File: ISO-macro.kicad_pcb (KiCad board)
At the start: 2 copper layers, 105.9 x 38.1 mm, 20 parts, among them J1 USB_C_Receptacle_USB2.0, SW1 SW_SPST, SW2 SW_SPST, SW3 SW_SPST, SW4 SW_SPST, SW5 SW_SPST, SW6 SW_SPST, SW7 SW_SPST, SW8 Rotary_Encoder_Switch, SW9 SW_SPST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

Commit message: add backlights, connect things
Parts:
- added C2: 100n, Capacitor_SMD:C_0402_1005Metric, B.Cu at (129.0, 75.3)
- added C3: 100n, Capacitor_SMD:C_0402_1005Metric, B.Cu at (129.0, 79.4)
- added C4: 100nF, Capacitor_SMD:C_0402_1005Metric, B.Cu at (141.6, 77.0)
- added C5: 100nF, Capacitor_SMD:C_0402_1005Metric, B.Cu at (173.0, 77.2)
- added C6: 100nF, Capacitor_SMD:C_0402_1005Metric, B.Cu at (188.0, 77.6)
- added D1: WS2812B, LED_SMD:LED_WS2812B_PLCC4_5.0x5.0mm_P3.2mm, B.Cu at (136.3, 77.3)
- added D2: WS2812B, LED_SMD:LED_WS2812B_PLCC4_5.0x5.0mm_P3.2mm, B.Cu at (168.1, 77.3)
- added D3: WS2812B, LED_SMD:LED_WS2812B_PLCC4_5.0x5.0mm_P3.2mm, B.Cu at (192.4, 77.3)
- added R7: 10k, Resistor_SMD:R_0402_1005Metric, B.Cu at (117.5, 74.9)
- added R8: 10k, Resistor_SMD:R_0402_1005Metric, B.Cu at (117.5, 79.9)
- SW8: value Rotary_Encoder_Switch -> EC11
- moved SW9 3.78 mm to (186.5, 71.6)
- moved R4 0.67 mm to (120.3, 92.1)
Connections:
- SW8 pad A: Net-(SW8-PadA) -> /EncA
- SW8 pad B: Net-(SW8-PadB) -> /EncB
- SW8 pad C: Net-(SW8-PadC) -> GND
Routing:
- net VCC: track 83.9 -> 172.2 mm
- net GND: track 43.1 -> 87.2 mm
- net Net-(D1-Pad2): track 0.00 -> 28.3 mm
- net Net-(D2-Pad2): track 0.00 -> 20.7 mm
- net /EncB: track 0.00 -> 11.1 mm, vias 0 -> 1
- net /EncA: track 0.00 -> 11.1 mm, vias 0 -> 1
- net /Reset: track 70.9 -> 74.6 mm
- net Net-(R4-Pad2): track 1.57 -> 2.24 mm
- net Net-(SW2-Pad2): track 37.3 -> 37.9 mm
- net Net-(SW4-Pad2): track 54.0 -> 54.5 mm

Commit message: updated MCU, removed filter for rot enc
updated MCU, removed filter for rot enc
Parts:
- removed C2, C3: 100n, Capacitor_SMD:C_0402_1005Metric
- removed R7, R8: 10k, Resistor_SMD:R_0402_1005Metric
- U1: value ATmega16U4-MU -> ATmega16U2-MU; footprint Package_DFN_QFN:QFN-44-1EP_7x7mm_P0.5mm_EP5.2x5.2mm -> Package_DFN_QFN:QFN-32-1EP_5x5mm_P0.5mm_EP3.1x3.1mm
- moved U1 0.06 mm to (125.5, 88.6), turned to 0 degrees
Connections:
- R4 pad 1: GND -> /LED
- SW8 pad S2: Net-(SW8-PadS2) -> /encsw
- U1 pad 1: Net-(U1-Pad1) -> /Res1
- U1 pad 13: /Reset -> Net-(R4-Pad2)
- U1 pad 14: VCC -> Net-(SW7-Pad2)
- U1 pad 15: GND -> Net-(SW6-Pad2)
- U1 pad 16: /Res2 -> Net-(SW4-Pad2)
- U1 pad 17: /Res1 -> Net-(U1-Pad17)
- U1 pad 19: Net-(U1-Pad19) -> Net-(SW2-Pad2)
- U1 pad 2: VCC -> /Res2
- U1 pad 20: Net-(U1-Pad20) -> /encsw
- U1 pad 23: GND -> Net-(SW1-Pad2)
- U1 pad 24: VCC -> /Reset
- U1 pad 25: Net-(SW1-Pad2) -> Net-(U1-Pad25)
- U1 pad 26: Net-(SW3-Pad2) -> /EncB
- U1 pad 27: Net-(SW5-Pad2) -> Net-(C1-Pad1)
- U1 pad 28: Net-(SW7-Pad2) -> GND
- U1 pad 29: Net-(SW6-Pad2) -> Net-(R2-Pad1)
- U1 pad 3: Net-(R3-Pad1) -> GND
- U1 pad 30: Net-(SW4-Pad2) -> Net-(R3-Pad1)
- U1 pad 31: Net-(SW2-Pad2) -> VCC
- U1 pad 32: Net-(SW8-PadS2) -> VCC
- U1 pad 33: Net-(R4-Pad2) -> GND
- U1 pad 4: Net-(R2-Pad1) -> VCC
- U1 pad 5: GND -> /EncA
- U1 pad 6: Net-(C1-Pad1) -> Net-(SW3-Pad2)
- U1 pad 7: VCC -> Net-(SW5-Pad2)
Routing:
- net /LED: track 0.00 -> 40.0 mm, vias 0 -> 2
- net Net-(SW8-PadS2): track 21.0 -> 0.00 mm
- net /encsw: track 0.00 -> 21.0 mm
- net /EncB: track 11.1 -> 0.00 mm, vias 1 -> 0
- net /EncA: track 11.1 -> 0.00 mm, vias 1 -> 0
- net GND: track 87.2 -> 82.9 mm, vias 6 -> 5
- net VCC: track 172.2 -> 169.2 mm

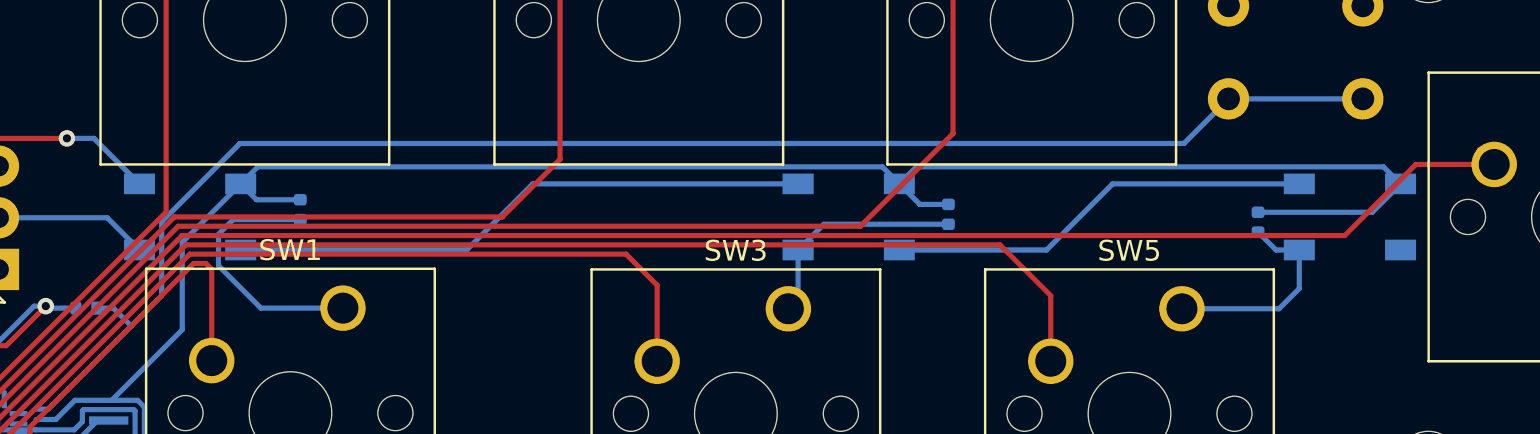
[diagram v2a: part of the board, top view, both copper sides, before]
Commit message: add bom list
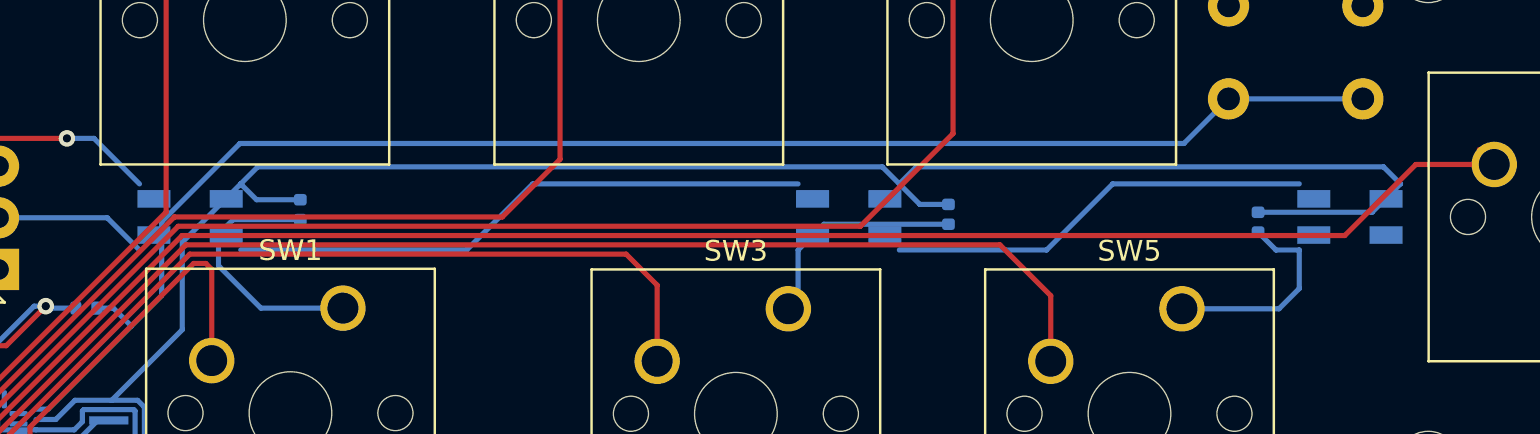
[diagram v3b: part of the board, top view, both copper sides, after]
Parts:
- D1, D2, D3: footprint LED_SMD:LED_WS2812B_PLCC4_5.0x5.0mm_P3.2mm -> LED_SMD:LED_SK6812MINI_PLCC4_3.5x3.5mm_P1.75mm
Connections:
- D3 pad 2: Net-(D3-Pad2) -> (no net)
- J1 pad A8: Net-(J1-PadA8) -> (no net)
- J1 pad B8: Net-(J1-PadB8) -> (no net)
- U1 pad 10: Net-(U1-Pad10) -> (no net)
- U1 pad 11: Net-(U1-Pad11) -> (no net)
- U1 pad 12: Net-(U1-Pad12) -> (no net)
- U1 pad 17: Net-(U1-Pad17) -> (no net)
- U1 pad 18: Net-(U1-Pad18) -> (no net)
- U1 pad 21: Net-(U1-Pad21) -> (no net)
- U1 pad 22: Net-(U1-Pad22) -> (no net)
- U1 pad 25: Net-(U1-Pad25) -> (no net)
- U1 pad 8: Net-(U1-Pad8) -> (no net)
- U1 pad 9: Net-(U1-Pad9) -> (no net)

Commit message: Update ISO-macro.kicad_pcb
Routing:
- net VCC: track 169.2 -> 0.00 mm
- net Net-(SW7-Pad2): track 89.4 -> 0.00 mm
- net GND: track 82.9 -> 0.00 mm
- net /Reset: track 74.6 -> 0.00 mm
- net Net-(SW6-Pad2): track 71.7 -> 0.00 mm
- net Net-(SW5-Pad2): track 68.8 -> 0.00 mm
- net Net-(SW4-Pad2): track 54.5 -> 0.00 mm
- net Net-(SW3-Pad2): track 49.1 -> 0.00 mm
- net /LED: track 40.0 -> 0.00 mm
- net Net-(SW2-Pad2): track 37.9 -> 0.00 mm
- net Net-(D1-Pad2): track 28.3 -> 0.00 mm
- net Net-(SW1-Pad2): track 27.0 -> 0.00 mm
- net /encsw: track 21.0 -> 0.00 mm
- net Net-(D2-Pad2): track 20.7 -> 0.00 mm
- net Net-(R3-Pad1): track 13.6 -> 0.00 mm
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
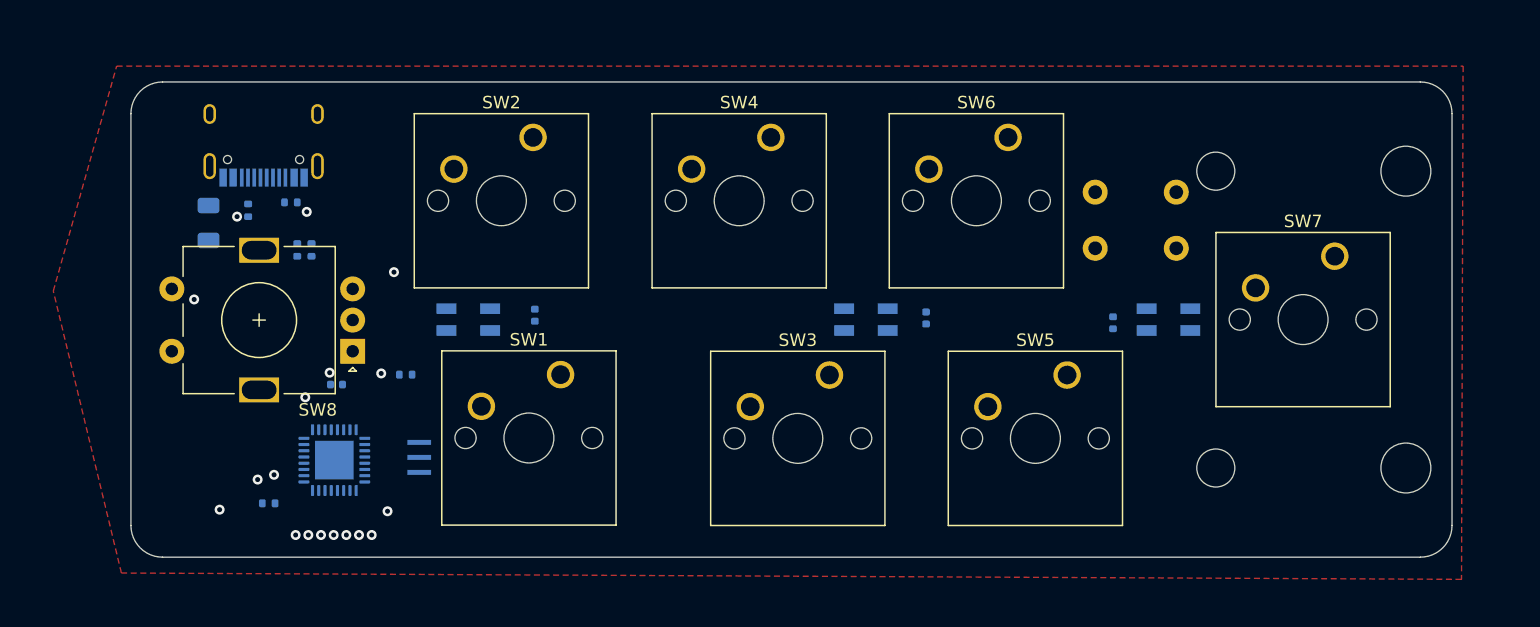
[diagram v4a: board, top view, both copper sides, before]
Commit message: Add power caps, LEDs, finish routing (#3)
* wip

* Add LEDs and power caps, routing

* rm unuseds

* Add NCs where appropriate
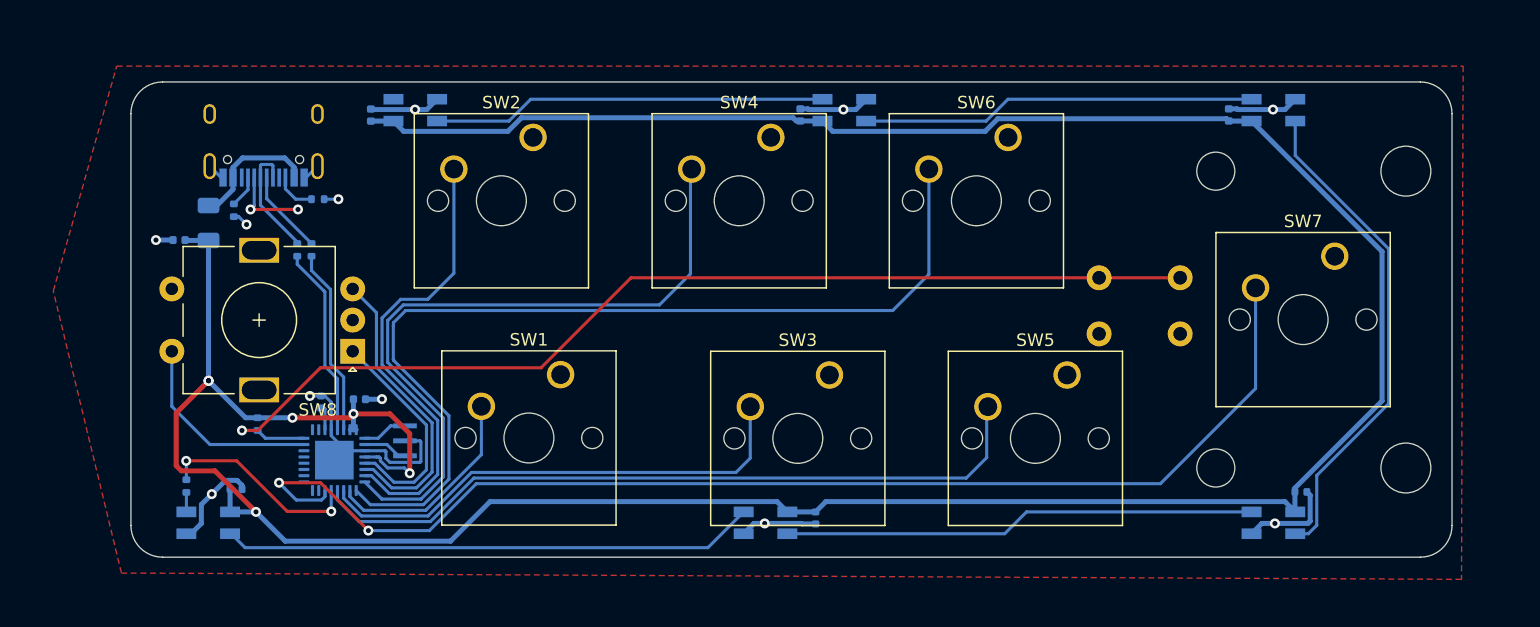
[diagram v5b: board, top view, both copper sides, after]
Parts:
- added C2: 100nF, Capacitor_SMD:C_0402_1005Metric, B.Cu at (128.5, 60.9)
- added C3: 100nF, Capacitor_SMD:C_0402_1005Metric, B.Cu at (197.2, 60.9)
- added C7: 100nF, Capacitor_SMD:C_0402_1005Metric, B.Cu at (162.9, 60.9)
- added C8: 10uF, Capacitor_SMD:C_0402_1005Metric, B.Cu at (113.1, 71.0)
- added C9: 100nF, Capacitor_SMD:C_0402_1005Metric, B.Cu at (127.5, 83.7)
- added D4: WS2812B, LED_SMD:LED_SK6812MINI_PLCC4_3.5x3.5mm_P1.75mm, B.Cu at (200.8, 60.6)
- added D5: WS2812B, LED_SMD:LED_SK6812MINI_PLCC4_3.5x3.5mm_P1.75mm, B.Cu at (166.4, 60.6)
- added D6: WS2812B, LED_SMD:LED_SK6812MINI_PLCC4_3.5x3.5mm_P1.75mm, B.Cu at (132.0, 60.6)
- moved C5 33.1 mm to (203.0, 91.2), turned to 0 degrees
- moved C6 28.5 mm to (164.1, 93.2)
- moved C4 27.7 mm to (117.7, 90.9), turned to 0 degrees
- moved D1 26.5 mm to (115.4, 93.6)
- moved D3 18.3 mm to (200.8, 93.6)
- moved D2 18.2 mm to (160.1, 93.6)
- moved R1 12.5 mm to (119.4, 85.7), turned to 270 degrees
- moved SW9 7.21 mm to (193.3, 74.0), turned to 180 degrees
- moved R4 6.75 mm to (113.7, 90.7), turned to 90 degrees
- moved R6 2.17 mm to (124.2, 67.7)
- moved C1 1.87 mm to (124.5, 83.9), turned to 90 degrees
- moved Y1 1.75 mm to (131.2, 87.1), turned to 270 degrees
- moved R2 1.14 mm to (122.6, 71.8)
- moved R3 1.14 mm to (123.7, 71.8)
- moved R5 1.14 mm to (117.5, 68.6)
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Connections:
- D3 pad 2: (no net) -> Net-(D3-Pad2)
- U1 pad 10: (no net) -> Net-(SW1-Pad2)
- U1 pad 11: (no net) -> Net-(SW3-Pad2)
- U1 pad 12: (no net) -> Net-(SW5-Pad2)
- U1 pad 15: Net-(SW6-Pad2) -> (no net)
- U1 pad 16: Net-(SW4-Pad2) -> (no net)
- U1 pad 19: Net-(SW2-Pad2) -> (no net)
- U1 pad 20: /encsw -> (no net)
- U1 pad 23: Net-(SW1-Pad2) -> /encsw
- U1 pad 26: /EncB -> (no net)
- U1 pad 6: Net-(SW3-Pad2) -> /EncB
- U1 pad 7: Net-(SW5-Pad2) -> Net-(SW2-Pad2)
- U1 pad 8: (no net) -> Net-(SW4-Pad2)
- U1 pad 9: (no net) -> Net-(SW6-Pad2)
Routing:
- net VCC: track 0.00 -> 258.9 mm, vias 4 -> 6
- net Net-(SW7-Pad2): track 0.00 -> 97.5 mm, vias 1 -> 2
- net /Reset: track 0.00 -> 85.5 mm, vias 0 -> 1
- net Net-(SW6-Pad2): track 0.00 -> 76.1 mm, vias 1 -> 0
- net GND: track 0.00 -> 62.2 mm, vias 5 -> 11
- net Net-(SW5-Pad2): track 0.00 -> 59.8 mm, vias 1 -> 0
- net Net-(SW4-Pad2): track 0.00 -> 56.3 mm, vias 1 -> 0
- net Net-(D1-Pad2): track 0.00 -> 42.8 mm
- net Net-(D3-Pad2): track 0.00 -> 39.9 mm
- net Net-(SW3-Pad2): track 0.00 -> 39.9 mm, vias 1 -> 0
- net Net-(D2-Pad2): track 0.00 -> 37.9 mm
- net Net-(SW2-Pad2): track 0.00 -> 37.1 mm, vias 1 -> 0
- net Net-(D4-Pad2): track 0.00 -> 31.6 mm
- net Net-(D5-Pad2): track 0.00 -> 31.6 mm
- net /EncB: track 0.00 -> 23.9 mm
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
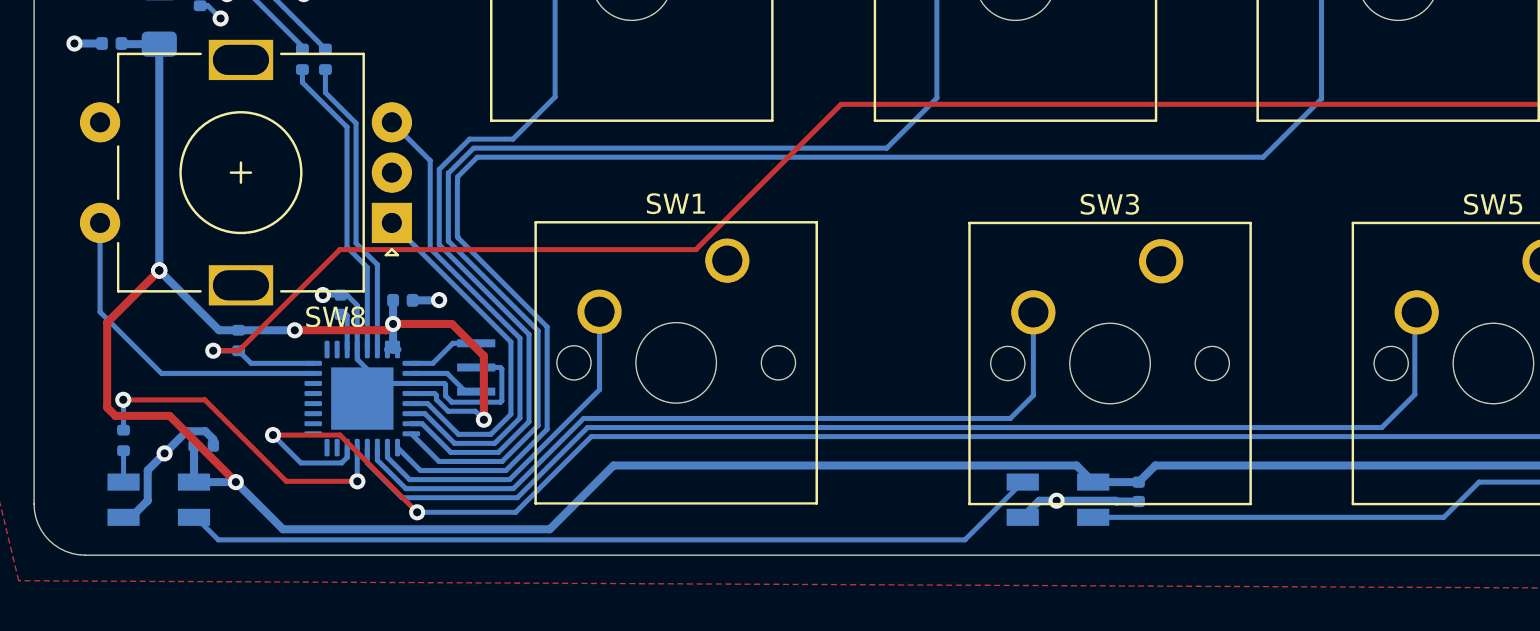
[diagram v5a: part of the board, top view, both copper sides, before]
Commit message: update bom, change from integrated resonator to crystal
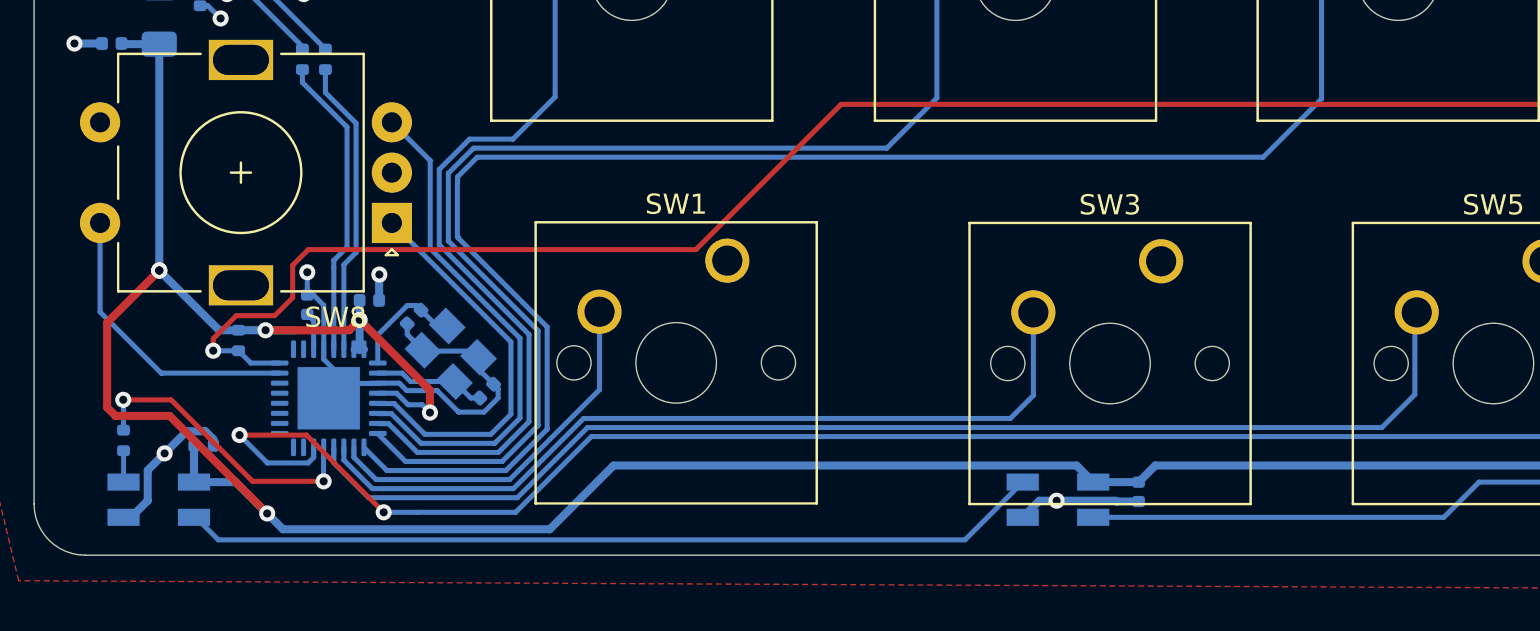
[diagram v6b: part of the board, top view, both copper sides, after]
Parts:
- added C10: 22pF, Capacitor_SMD:C_0402_1005Metric, B.Cu at (128.1, 84.6)
- added C11: 22pF, Capacitor_SMD:C_0402_1005Metric, B.Cu at (131.7, 88.2)
- Y1: value Resonator -> Crystal_GND24; footprint Crystal:Resonator_SMD_muRata_CSTxExxV-3Pin_3.0x1.1mm -> Crystal:Crystal_SMD_3225-4Pin_3.2x2.5mm
- moved U1 1.67 mm to (123.9, 88.6)
- moved C1 1.66 mm to (122.8, 83.9)
- moved C9 1.66 mm to (125.9, 83.7)
- moved Y1 1.43 mm to (129.9, 86.4), turned to 315 degrees
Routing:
- net GND: track 62.2 -> 68.1 mm
- net /Res1: track 3.64 -> 5.87 mm
- net /Res2: track 3.60 -> 5.58 mm
- net Net-(R4-Pad2): track 16.5 -> 14.8 mm
- net /EncA: track 18.0 -> 19.6 mm
- net Net-(SW4-Pad2): track 56.3 -> 57.9 mm
- net Net-(SW1-Pad2): track 17.2 -> 18.9 mm
- net /EncB: track 23.9 -> 25.5 mm
- net Net-(SW3-Pad2): track 39.9 -> 41.5 mm
- net Net-(SW7-Pad2): track 97.5 -> 99.2 mm
- net Net-(SW5-Pad2): track 59.8 -> 61.4 mm
- net Net-(SW6-Pad2): track 76.1 -> 77.8 mm
- net Net-(SW2-Pad2): track 37.1 -> 38.7 mm
- net /encsw: track 16.3 -> 14.6 mm
- net VCC: track 258.9 -> 257.4 mm
